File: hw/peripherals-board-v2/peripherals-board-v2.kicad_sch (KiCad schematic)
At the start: 0 parts

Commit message: Add library for RP2040-zero
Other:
- note added: "Requirements: Waveshare RP2040-Zero On-board MPU6050/BNO055 (Options for both) EEPROM chip to store log data (MicroSD too big) OLED for status (ext connector, might need to mount OLED on top of frame) TB6612FNG Motor Driver Three I2C ports for LiDAR sensor Screw Terminal for power input Screw terminal for motor output Connector for steering servo break out GPIO"
- company: (none) -> DIY Laboratories
- title: (none) -> Peripherals Board V2
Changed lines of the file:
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@@
 	(generator_version "9.0")
 	(paper "A4")
+	(title_block
+		(title "Peripherals Board V2")
+		(date "2025-07-07")
+		(rev "2")
+		(company "DIY Laboratories")
+	)
+	(text "Requirements:\nWaveshare RP2040-Zero\nOn-board MPU6050/BNO055 (Options for both)\nEEPROM chip to store log data (MicroSD too big)\nOLED for status (ext connector, might need to mount OLED on top of frame)\nTB6612FNG Motor Driver\nThree I2C ports for LiDAR sensor\nScrew Terminal for power input\nScrew terminal for motor output\nConnector for steering servo\nbreak out GPIO"
+		(exclude_from_sim no)
+		(at 55.88 28.194 0)
+		(effects
+			(font
+				(size 1.27 1.27)
+			)
+		)
+	)
 	(sheet_instances
 		(path "/"

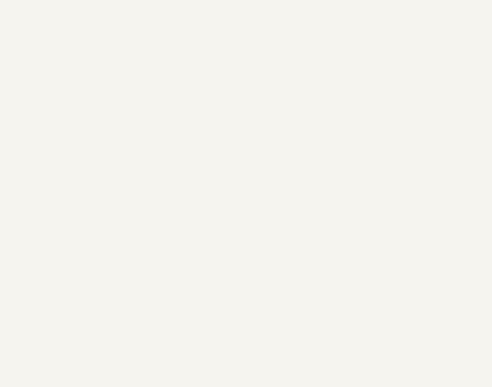
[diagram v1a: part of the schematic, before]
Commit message: Create symbol and footprint for TB6612 breakout board
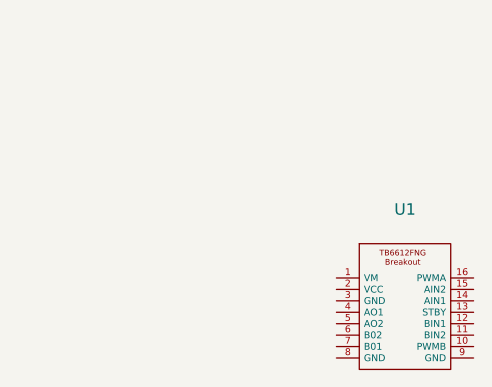
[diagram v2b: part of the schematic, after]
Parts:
- added U1: ~, symbol TB6612FNG-breakout:TB6612FNG-breakout
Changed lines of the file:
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@@
+		)
+	)
+	(symbol
+		(lib_id "TB6612FNG-breakout:TB6612FNG-breakout")
+		(at 146.05 49.53 0)
+		(unit 1)
+		(exclude_from_sim no)
+		(in_bom yes)
+		(on_board yes)
+		(dnp no)
+		(fields_autoplaced yes)
+		(property "Reference" "U1"
+			(at 153.67 44.45 0)
+			(effects
+				(font
+					(size 1.27 1.27)
+				)
+			)
+		)
+		(property "Value" "~"
+			(at 153.67 46.99 0)
+			(effects
+				(font
+					(size 1.27 1.27)
+				)
+			)
+		)
+		(property "Footprint" ""
+			(at 146.05 49.53 0)
+			(effects
+				(font
+					(size 1.27 1.27)
+				)
+				(hide yes)
+			)
+		)
+		(property "Datasheet" ""
+			(at 146.05 49.53 0)
+			(effects
+				(font
+					(size 1.27 1.27)
+				)
+				(hide yes)
+			)
+		)
+		(property "Description" ""
+			(at 146.05 49.53 0)
+			(effects
+				(font
+					(size 1.27 1.27)
+				)
+				(hide yes)
+			)
+		)
+		(pin "2"
+		)
+		(pin "7"
+		)
+		(pin "15"
+		)
+		(pin "6"
+		)
+		(pin "13"
+		)
+		(pin "1"
+		)
+		(pin "9"
+		)
+		(pin "12"
+		)
+		(pin "5"
+		)
+		(pin "4"
+		)
+		(pin "8"
+		)
+		(pin "16"
+		)
+		(pin "14"
+		)
+		(pin "11"
+		)
+		(pin "10"
+		)
+		(pin "3"
+		)
+		(instances
+			(project ""
+				(path "/caa19d1a-d407-4cf5-a8f8-de116332f63c"
+					(reference "U1")
+					(unit 1)
+				)
+			)
 		)
 	)

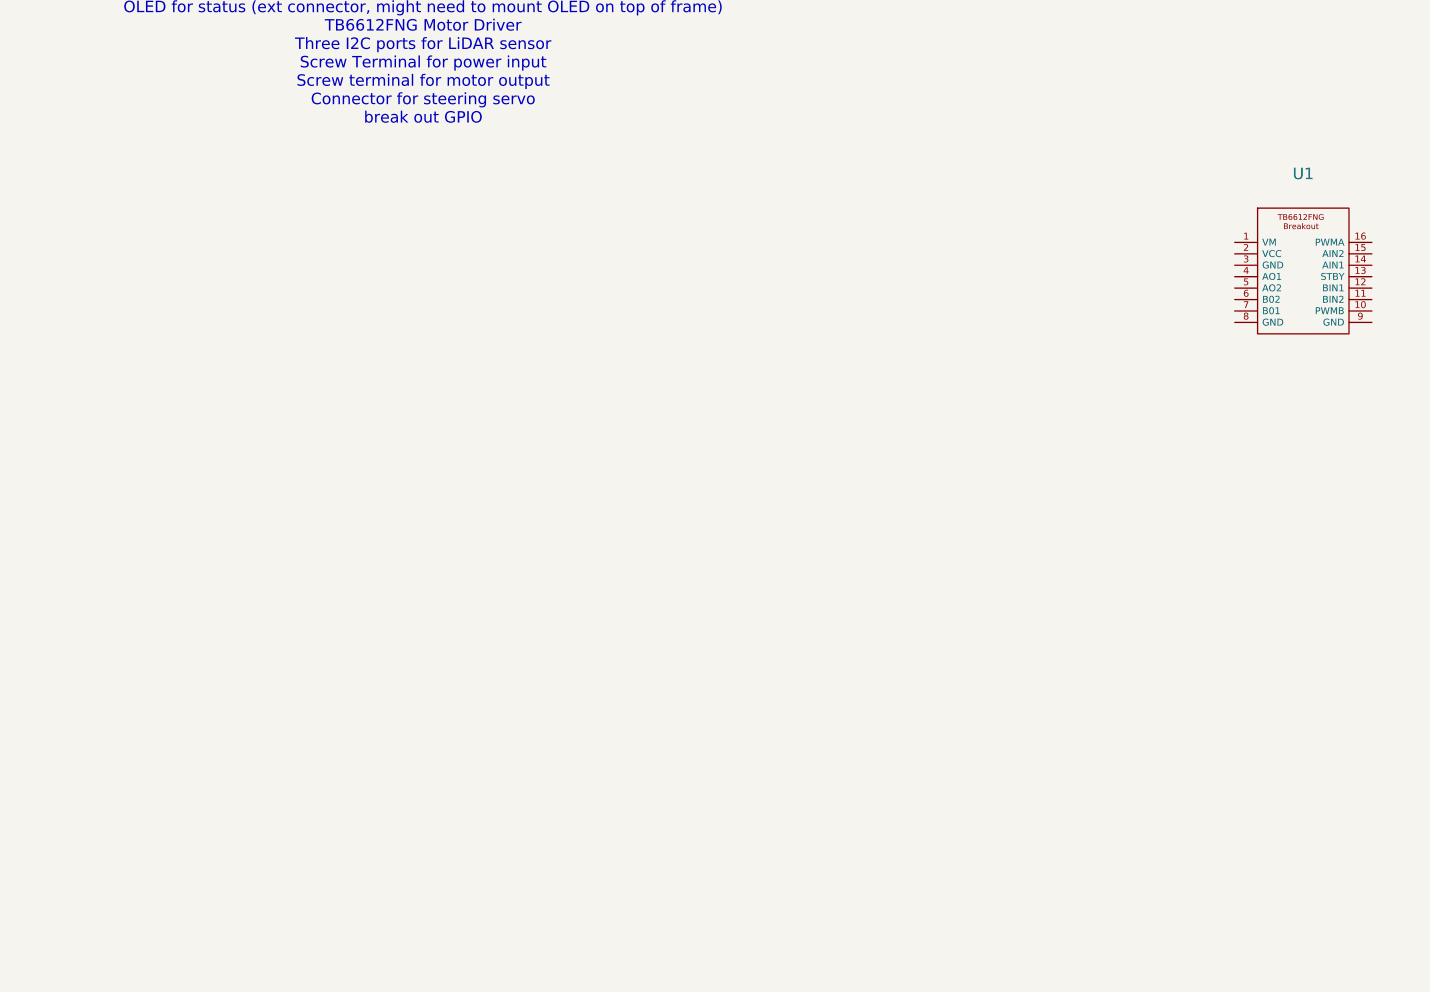
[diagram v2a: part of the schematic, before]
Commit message: Create symbol and footprint for GY-87
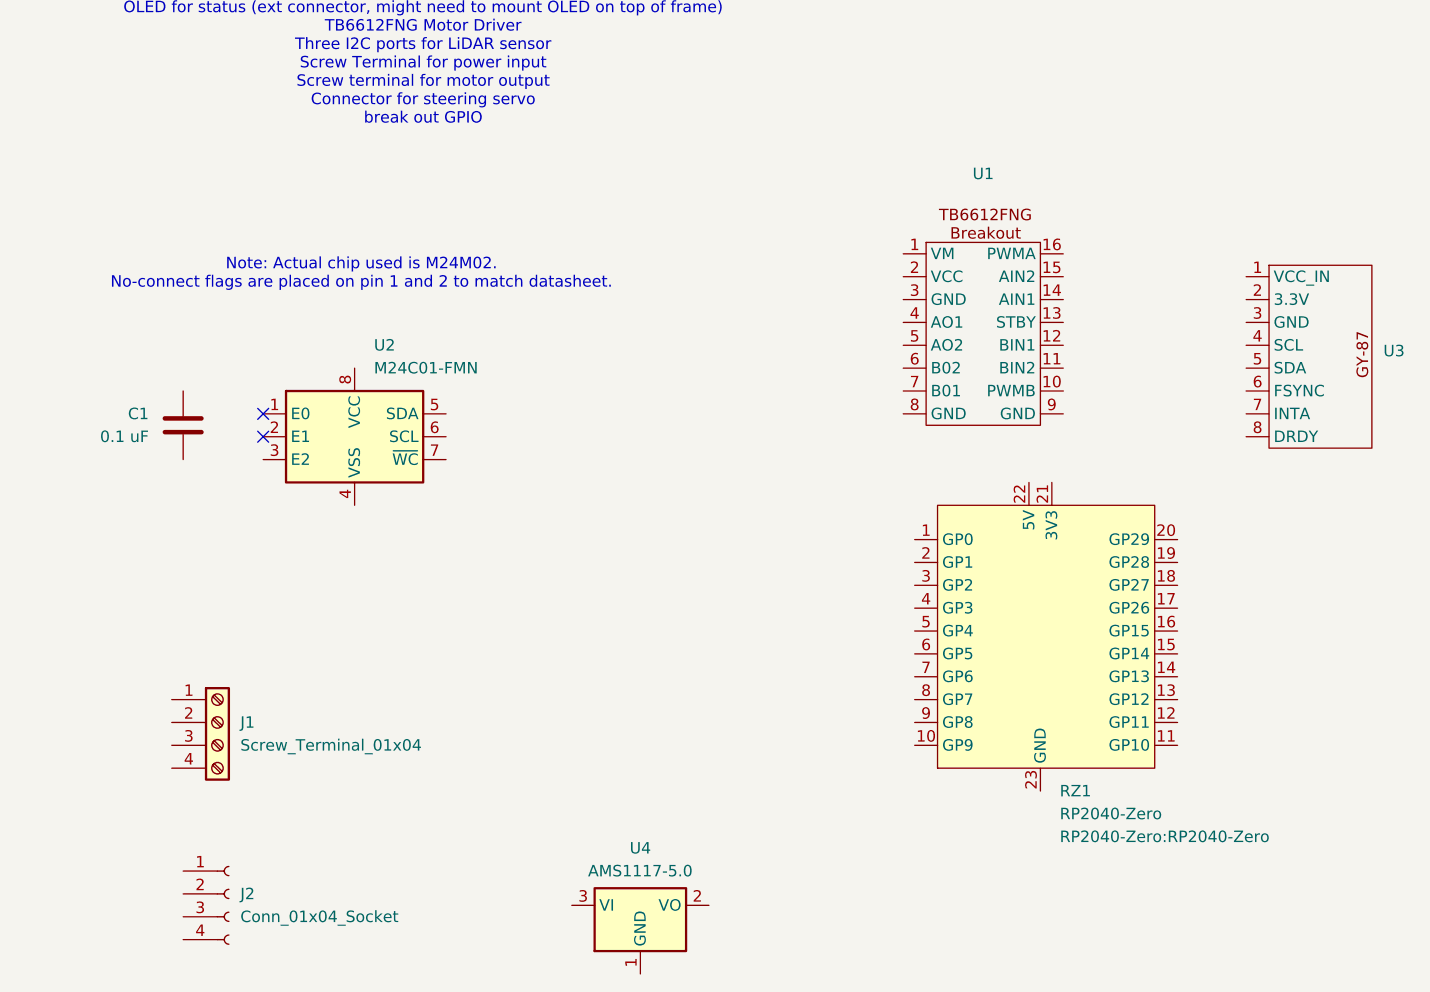
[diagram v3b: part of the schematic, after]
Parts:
- added C1: 0.1 uF, Capacitor_SMD:C_0805_2012Metric_Pad1.18x1.45mm_HandSolder, symbol Device:C
- added J1: Screw_Terminal_01x04, TerminalBlock_RND:TerminalBlock_RND_205-00047_1x04_P5.00mm_Horizontal, symbol Connector:Screw_Terminal_01x04
- added J2: Conn_01x04_Socket, Connector_JST:JST_EH_S4B-EH_1x04_P2.50mm_Horizontal, symbol Connector:Conn_01x04_Socket
- added RZ1: RP2040-Zero, RP2040-Zero:RP2040-Zero, symbol rp2040-zero:RP2040-Zero
- added U2: M24C01-FMN, Package_SO:SOIC-8_3.9x4.9mm_P1.27mm, symbol Memory_EEPROM:M24C01-FMN
- added U3: ~, symbol GY87:GY87
- added U4: AMS1117-5.0, Package_TO_SOT_SMD:TO-263-2, symbol Regulator_Linear:AMS1117-5.0
- U1: footprint (none) -> TB6612FNG-breakout:TB6612FNG-breakout
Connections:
- no-connect marks 0 -> 2
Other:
- note added: "Note: Actual chip used is M24M02. No-connect flags are placed on pin 1 and 2 to match datasheet."

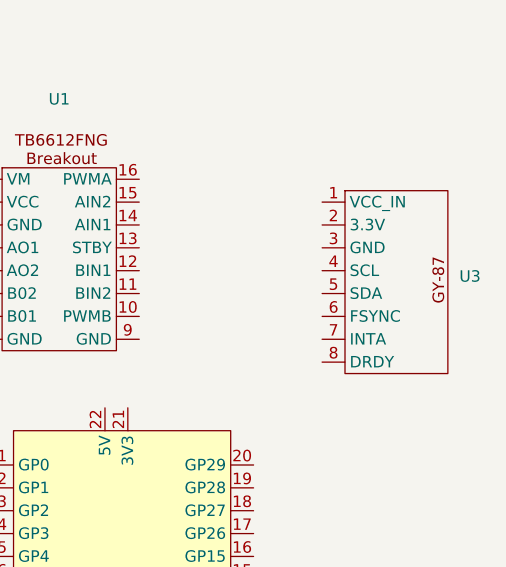
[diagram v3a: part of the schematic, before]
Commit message: Link GY87 footprint to symbol
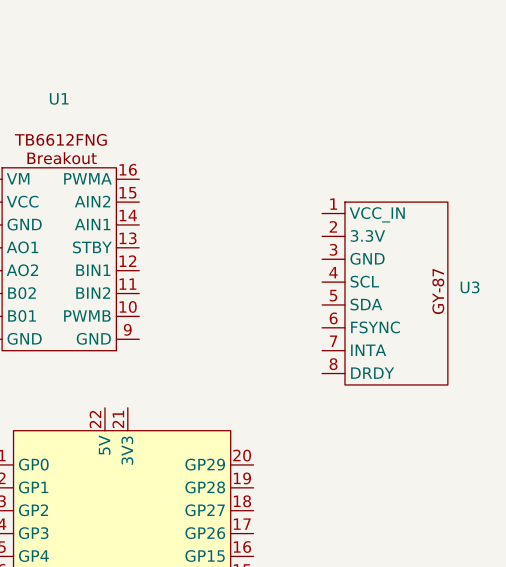
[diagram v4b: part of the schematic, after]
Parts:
- U3: footprint (none) -> GY87:GY87
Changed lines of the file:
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@@
+	)
+	(symbol
+		(lib_id "GY87:GY87")
+		(at 146.05 54.61 0)
+		(unit 1)
+		(exclude_from_sim no)
+		(in_bom yes)
+		(on_board yes)
+		(dnp no)
+		(fields_autoplaced yes)
+		(property "Reference" "U3"
+			(at 162.56 65.4049 0)
+			(effects
+				(font
+					(size 1.27 1.27)
+				)
+				(justify left)
+			)
+		)
+		(property "Value" "~"
+			(at 162.56 67.31 0)
+			(effects
+				(font
+					(size 1.27 1.27)
+				)
+				(justify left)
+			)
+		)
+		(property "Footprint" "GY87:GY87"
+			(at 146.05 54.61 0)
+			(effects
+				(font
+					(size 1.27 1.27)
+				)
+				(hide yes)
+			)
+		)
+		(property "Datasheet" ""
+			(at 146.05 54.61 0)
+			(effects
+				(font
+					(size 1.27 1.27)
+				)
+				(hide yes)
+			)
+		)
+		(property "Description" ""
+			(at 146.05 54.61 0)
+			(effects
+				(font
+					(size 1.27 1.27)
+				)
+				(hide yes)
+			)
+		)
+		(pin "1"
+		)
+		(pin "4"
+		)
+		(pin "6"
+		)
+		(pin "2"
+		)
+		(pin "3"
+		)
+		(pin "5"
+		)
+		(pin "7"
+		)
+		(pin "8"
+		)
+		(instances
+			(project ""
+				(path "/caa19d1a-d407-4cf5-a8f8-de116332f63c"
+					(reference "U3")
+					(unit 1)
+				)
+			)
+		)
 	)
 	(symbol
@@
 					(unit 1)
 				)
-			)
-		)
-	)
-	(symbol
-		(lib_id "GY87:GY87")
-		(at 146.05 53.34 0)
-		(unit 1)
-		(exclude_from_sim no)
-		(in_bom yes)
-		(on_board yes)
-		(dnp no)
-		(fields_autoplaced yes)
-		(property "Reference" "U3"
-			(at 162.56 64.1349 0)
-			(effects
-				(font
-					(size 1.27 1.27)
-				)
-				(justify left)
-			)
-		)
-		(property "Value" "~"
-			(at 162.56 66.04 0)
-			(effects
-				(font
-					(size 1.27 1.27)
-				)
-				(justify left)
-			)
-		)
-		(property "Footprint" ""
-			(at 146.05 53.34 0)
-			(effects
-				(font
-					(size 1.27 1.27)
-				)
-				(hide yes)
-			)
-		)
-		(property "Datasheet" ""
-			(at 146.05 53.34 0)
-			(effects
-				(font
-					(size 1.27 1.27)
-				)
-				(hide yes)
-			)
-		)
-		(property "Description" ""
-			(at 146.05 53.34 0)
-			(effects
-				(font
-					(size 1.27 1.27)
-				)
-				(hide yes)
-			)
-		)
-		(pin "4"
-		)
-		(pin "2"
-		)
-		(pin "5"
-		)
-		(pin "6"
-		)
-		(pin "3"
-		)
-		(pin "1"
-		)
-		(pin "7"
-		)
-		(pin "8"
-		)
-		(instances
-			(project ""
-				(path "/caa19d1a-d407-4cf5-a8f8-de116332f63c"
-					(reference "U3")
-					(unit 1)
-				)
